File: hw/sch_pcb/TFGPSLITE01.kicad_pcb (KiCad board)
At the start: 4 copper layers, 49.8 x 39.6 mm, 26 parts, among them IC1 CAM-M8Q, J1 SM06B-GHS-TB, J2 SM04B-GHS-TB, M1 HOLE, M2 HOLE, M3 HOLE, M4 HOLE, U1 MIC5504-3.3YM5

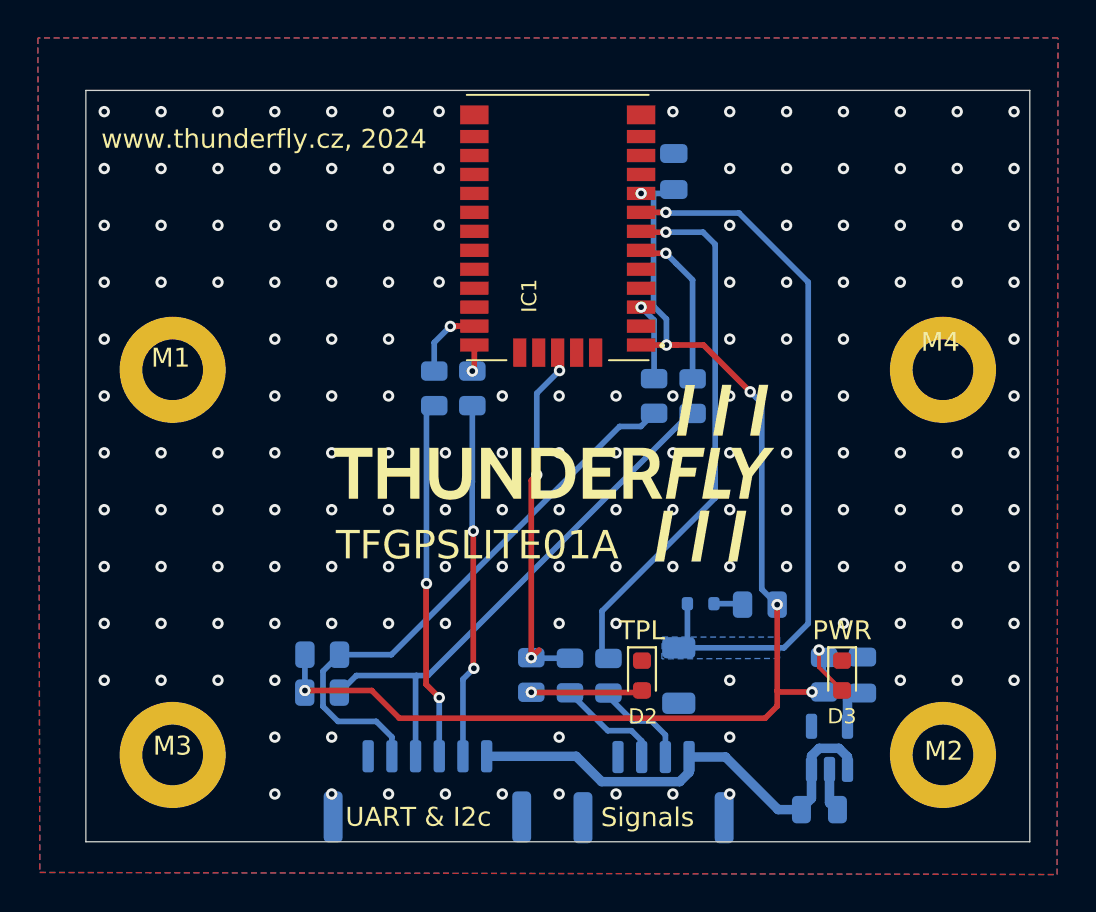
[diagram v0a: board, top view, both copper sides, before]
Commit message: solve DRC, silkscreen
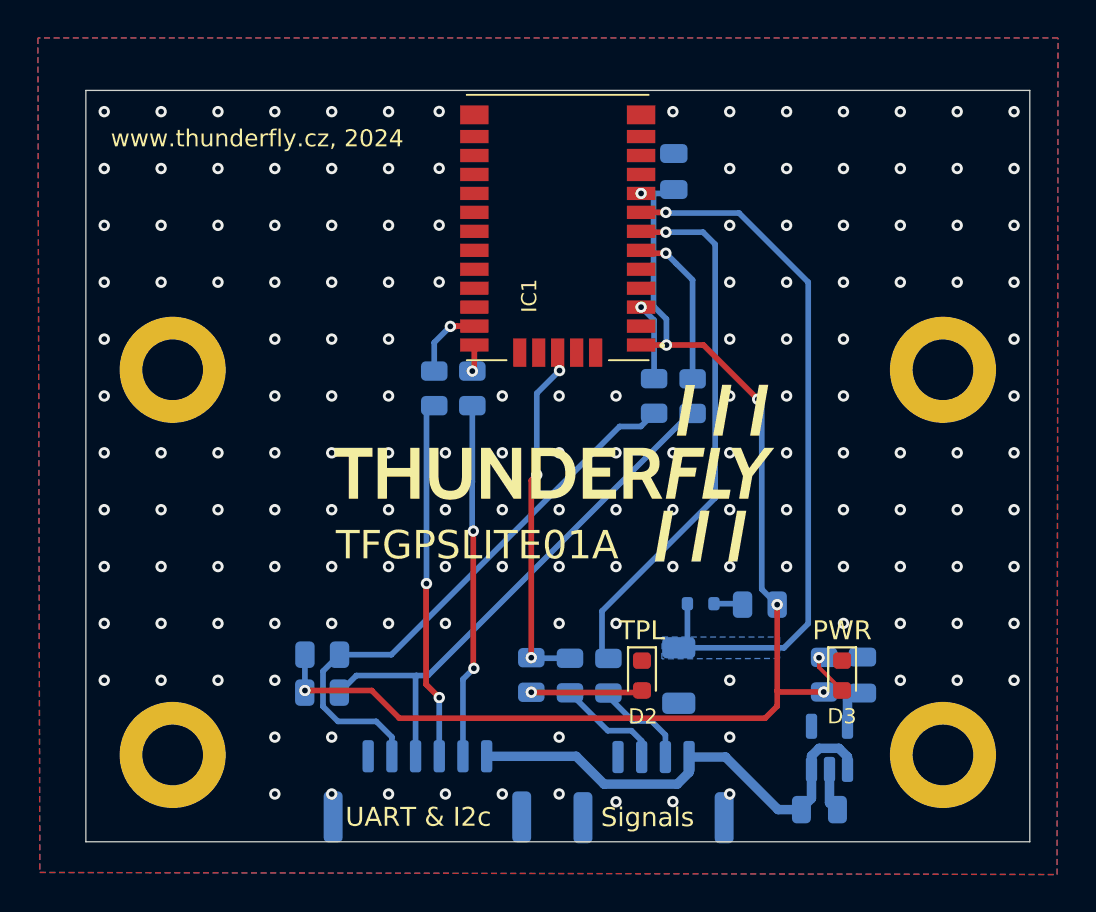
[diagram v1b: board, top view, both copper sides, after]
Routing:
- net Net-(D3-A): track 3.45 -> 2.23 mm
- net /TPL: track 19.5 -> 18.9 mm
- net GND: vias 158 -> 157
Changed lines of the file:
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@@
 			(at -0.14 -1.47 0)
 			(layer "F.SilkS")
+			(hide yes)
 			(effects
 				(font
@@
 			(at -0.11 -0.63 0)
 			(layer "F.SilkS")
+			(hide yes)
 			(effects
 				(font
@@
 			(at -0.01 -0.48 0)
 			(layer "F.SilkS")
+			(hide yes)
 			(effects
 				(font
@@
 			(at 0.04 -0.21 0)
 			(layer "F.SilkS")
+			(hide yes)
 			(effects
 				(font
@@
 	)
 	(gr_text "www.thunderfly.cz, 2024"
-		(at 111.93 88.25 0)
+		(at 112.43 88.16 0)
 		(layer "F.SilkS")
 		(effects
 			(font
-				(size 1 1)
+				(size 0.9 0.9)
 				(thickness 0.1)
 			)
@@
 	)
 	(segment
-		(start 147.5925 117.5875)
-		(end 147.59 117.59)
+		(start 150.045001 116.8375)
+		(end 147.66 116.8375)
 		(width 0.3)
 		(layer "F.Cu")
@@
 	)
 	(segment
-		(start 147.66 116.8375)
-		(end 147.5925 116.77)
+		(start 147.5925 117.5875)
+		(end 147.59 117.59)
 		(width 0.3)
 		(layer "F.Cu")
@@
 	)
 	(segment
-		(start 141.75 98.535)
-		(end 143.705 98.535)
-		(width 0.3)
-		(layer "F.Cu")
-		(net 1)
-	)
-	(segment
 		(start 146.96 118.22)
 		(end 147.59 117.59)
@@
 	)
 	(segment
-		(start 149.43 116.8375)
-		(end 147.66 116.8375)
+		(start 126.2 116.76)
+		(end 127.66 118.22)
 		(width 0.3)
 		(layer "F.Cu")
@@
 	)
 	(segment
-		(start 143.705 98.535)
-		(end 146.17 101)
+		(start 146.565 101.395)
+		(end 143.705 98.535)
 		(width 0.3)
 		(layer "F.Cu")
@@
 	)
 	(segment
-		(start 126.2 116.76)
-		(end 127.66 118.22)
+		(start 147.66 116.8375)
+		(end 147.5925 116.77)
 		(width 0.3)
 		(layer "F.Cu")
@@
 	)
 	(segment
-		(start 142.31 98.52)
-		(end 141.765 98.52)
+		(start 141.75 98.535)
+		(end 140.4135 98.535)
 		(width 0.3)
 		(layer "F.Cu")
@@
 	)
 	(segment
-		(start 141.75 98.535)
-		(end 140.4135 98.535)
+		(start 143.705 98.535)
+		(end 141.75 98.535)
 		(width 0.3)
 		(layer "F.Cu")
@@
 	)
 	(via
-		(at 149.43 116.8375)
+		(at 150.045001 116.8375)
 		(size 0.6)
 		(drill 0.3)
@@
 	)
 	(via
-		(at 146.17 101)
+		(at 146.565 101.395)
 		(size 0.6)
 		(drill 0.3)
@@
 	)
 	(segment
-		(start 146.78 101.61)
-		(end 146.17 101)
-		(width 0.3)
-		(layer "B.Cu")
-		(net 1)
-	)
-	(segment
 		(start 151.3025 117.245)
 		(end 151.6525 116.895)
@@
 	)
 	(segment
-		(start 146.78 111.4175)
-		(end 146.78 101.61)
-		(width 0.3)
-		(layer "B.Cu")
-		(net 1)
-	)
-	(segment
 		(start 151.6525 116.895)
 		(end 149.69 116.895)
@@
 	)
 	(segment
-		(start 147.5925 112.23)
+		(start 146.78 101.61)
 		(end 146.78 111.4175)
 		(width 0.3)
@@
 	)
 	(segment
+		(start 146.78 111.4175)
+		(end 147.5925 112.23)
+		(width 0.3)
+		(layer "B.Cu")
+		(net 1)
+	)
+	(segment
 		(start 140.4135 90.535)
 		(end 141.07 90.535)
@@
 	)
 	(segment
+		(start 146.565 101.395)
+		(end 146.78 101.61)
+		(width 0.3)
+		(layer "B.Cu")
+		(net 1)
+	)
+	(segment
 		(start 141.07 96.484394)
 		(end 141.07 90.535)
@@
 	)
 	(via
-		(at 142.09 101.22)
-		(size 0.6)
-		(drill 0.3)
-		(layers "F.Cu" "B.Cu")
-		(free yes)
-		(net 2)
-	)
-	(via
 		(at 112.09 110.22)
 		(size 0.6)
@@
 	)
 	(via
-		(at 139.09 122.22)
+		(at 139.09 122.63)
 		(size 0.6)
 		(drill 0.3)
@@
 	)
 	(via
-		(at 142.09 122.22)
+		(at 142.09 122.62)
 		(size 0.6)
 		(drill 0.3)
@@
 	)
 	(segment
-		(start 142.945 121.075)
-		(end 142.945 120.27)
+		(start 142.32 121.7)
+		(end 142.945 121.075)
 		(width 0.5)
 		(layer "B.Cu")
@@
 	)
 	(segment
-		(start 136.99 120.23)
-		(end 138.33 121.57)
+		(start 138.46 121.7)
+		(end 142.32 121.7)
 		(width 0.5)
 		(layer "B.Cu")
@@
 	)
 	(segment
-		(start 142.45 121.57)
-		(end 142.945 121.075)
+		(start 142.945 121.075)
+		(end 142.945 120.27)
 		(width 0.5)
 		(layer "B.Cu")
@@
 	)
 	(segment
-		(start 138.33 121.57)
-		(end 142.45 121.57)
+		(start 136.99 120.23)
+		(end 138.46 121.7)
 		(width 0.5)
 		(layer "B.Cu")
@@
 	)
 	(segment
-		(start 149.8 114.62)
+		(start 149.8 115.03)
 		(end 149.8 115.5375)
 		(width 0.2)
@@
 	)
 	(via
-		(at 149.8 114.62)
+		(at 149.8 115.03)
 		(size 0.6)
 		(drill 0.3)
@@
 	)
 	(segment
-		(start 150.07 115.695)
-		(end 150.16 115.785)
-		(width 0.2)
-		(layer "B.Cu")
-		(net 7)
-	)
-	(segment
-		(start 150.07 115.0125)
-		(end 150.07 115.695)
-		(width 0.2)
-		(layer "B.Cu")
-		(net 7)
-	)
-	(segment
 		(start 124.4925 116.87)
 		(end 125.3925 115.97)
@@
 		(width 0.3)
 		(layer "F.Cu")
-		(net 19)
-	)
-	(segment
-		(start 135.028001 114.619499)
-		(end 134.62 115.0275)
-		(width 0.3)
-		(layer "F.Cu")

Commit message: update actions
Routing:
- net /RF: track 0.00 -> 2.00 mm
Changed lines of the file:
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@@
 		(tags "resistor")
 		(property "Reference" "R7"
-			(at 2.73 0.01 360)
+			(at 2.73 0.01 0)
 			(layer "B.SilkS")
 			(effects
@@
 		)
 		(property "Value" "R_Small"
-			(at 0 -1.65 360)
+			(at 0 -1.65 0)
 			(layer "B.Fab")
 			(effects
@@
 		)
 		(fp_text user "${REFERENCE}"
-			(at 0 0 360)
+			(at 0 0 0)
 			(layer "B.Fab")
 			(effects
@@
 		(tags "Diode SOD523")
 		(property "Reference" "D1"
-			(at 0.0025 -1.46 360)
+			(at 0.0025 -1.46 0)
 			(layer "B.SilkS")
 			(effects
@@
 		)
 		(property "Value" "BZX585-B5V6.115"
-			(at 0 -1.4 360)
+			(at 0 -1.4 0)
 			(layer "B.Fab")
 			(effects
@@
 		)
 		(fp_text user "${REFERENCE}"
-			(at 0 1.3 360)
+			(at 0 1.3 0)
 			(layer "B.Fab")
 			(effects
@@
 		(tags "capacitor")
 		(property "Reference" "C3"
-			(at 2.7575 -0.015 360)
+			(at 2.7575 -0.015 0)
 			(layer "B.SilkS")
 			(effects
@@
 		)
 		(property "Value" "100n"
-			(at 0 -1.68 360)
+			(at 0 -1.68 0)
 			(layer "B.Fab")
 			(effects
@@
 		)
 		(fp_text user "${REFERENCE}"
-			(at 0 0 360)
+			(at 0 0 0)
 			(layer "B.Fab")
 			(effects
@@
 		(tags "resistor")
 		(property "Reference" "R8"
-			(at 2.59 0.01 360)
+			(at 2.59 0.01 0)
 			(layer "B.SilkS")
 			(effects
@@
 		)
 		(property "Value" "R_Small"
-			(at 0 -1.65 360)
+			(at 0 -1.65 0)
 			(layer "B.Fab")
 			(effects
@@
 		)
 		(fp_text user "${REFERENCE}"
-			(at 0 0 360)
+			(at 0 0 0)
 			(layer "B.Fab")
 			(effects
@@
 	)
 	(segment
+		(start 131.38 89.56)
+		(end 131.38 88.56)
+		(width 0.5)
+		(layer "F.Cu")
+		(net 12)
+	)
+	(segment
+		(start 131.87 89.53)
+		(end 131.87 88.53)
+		(width 0.5)
+		(layer "F.Cu")
+		(net 12)
+	)
+	(segment
